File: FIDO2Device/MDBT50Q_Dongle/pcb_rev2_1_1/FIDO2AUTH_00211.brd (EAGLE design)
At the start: 19.7 x 35.6 mm, 36 parts, among them CN1 TE-1734028, CN2 IF_4PIN, CN3 IF_3PIN_SOL, CN5 IF_2PIN_SOL, SW1 SKRPACE010, SW2 SKTADAE010, U1 MDBT50Q-P1M, U2 XC6206P332MR-G, X1 NX3215SA-32.768K

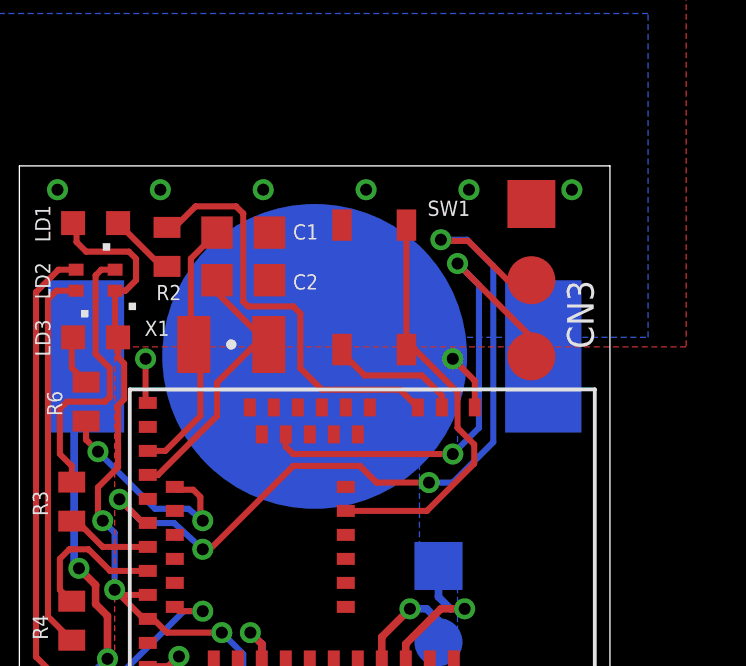
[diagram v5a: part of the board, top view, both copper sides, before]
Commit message: プリント基板設計データを修正
・TWIのブレイクアウトからGNDを削除（スペース削減のため）
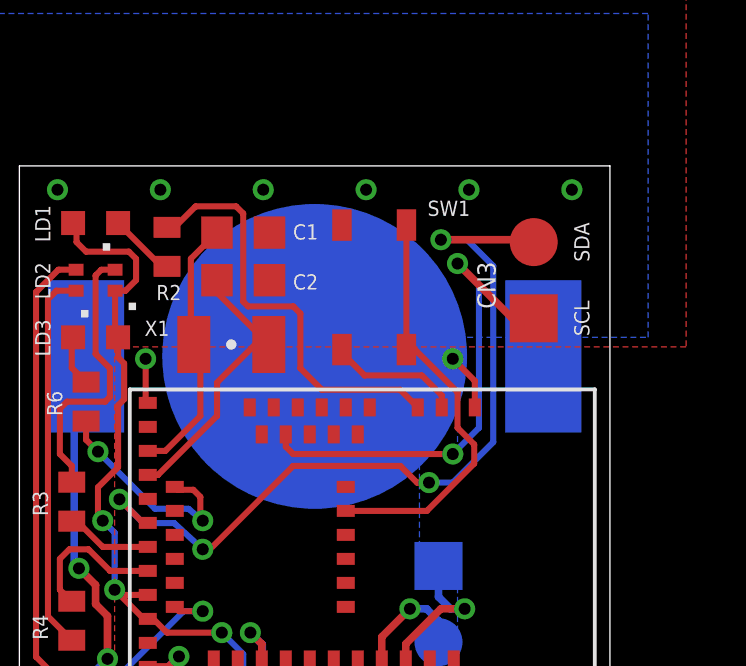
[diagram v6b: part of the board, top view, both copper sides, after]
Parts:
- CN3: value IF_3PIN_SOL -> IF_2PIN_SOL; device Connectors:SOLPAD_3PIN -> Connectors:SOLPAD_2PIN
- moved CN3 3.81 mm to (20.3, 30.5), turned to 90 degrees
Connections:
- net 0V: no longer CN3.1
- net TWI_SCL: now also CN3.1; no longer CN3.3
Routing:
- net TWI_SCL: track 17.2 -> 16.4 mm
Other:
- board text added: "SCL"
- board text added: "SDA"
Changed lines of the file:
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@@
 <setting verticaltext="up"/>
 </settings>
-<grid distance="0.05" unitdist="inch" unit="mil" style="lines" multiple="1" display="yes" altdistance="0.025" altunitdist="inch" altunit="inch"/>
+<grid distance="50" unitdist="mil" unit="mil" style="lines" multiple="1" display="yes" altdistance="0.025" altunitdist="inch" altunit="inch"/>
 <layers>
 <layer number="1" name="Top" color="4" fill="1" visible="yes" active="yes"/>
@@
 <text x="21.669375" y="14.605" size="0.508" layer="21" rot="R90" align="top-center">PCLK</text>
 <text x="21.669375" y="12.065" size="0.508" layer="21" rot="R90" align="top-center">PIO</text>
+<text x="21.669375" y="30.48" size="0.508" layer="21" rot="R90" align="top-center">SCL</text>
+<text x="21.669375" y="33.02" size="0.508" layer="21" rot="R90" align="top-center">SDA</text>
 </plain>
 <attributes>
@@
 </element>
 <element name="BAT1" library="Connectors" package="BAT-HLD-012-SMT" value="BAT-HLD-012-SMT" x="13.0175" y="29.21" rot="MR180"/>
-<element name="CN3" library="Connectors" package="SOLPAD_3PIN" value="IF_3PIN_SOL" x="20.240625" y="34.29" smashed="yes" rot="R270">
-<attribute name="NAME" x="21.43125" y="31.75" size="0.889" layer="25" ratio="11" rot="R270"/>
-<attribute name="VALUE" x="18.970625" y="35.56" size="0.889" layer="27" ratio="11" rot="R270" align="top-left"/>
-</element>
 <element name="LD3" library="Parts" package="CHIPLED_0603" value="APTD1608LSYCK" x="5.715" y="29.845" smashed="yes" rot="R180">
 <attribute name="NAME" x="4.206875" y="29.21" size="0.508" layer="25" rot="R90"/>
@@
 </element>
 <element name="CN5" library="Connectors" package="SOLPAD_2PIN" value="IF_2PIN_SOL" x="17.145" y="22.225" rot="MR270"/>
+<element name="CN3" library="Connectors" package="SOLPAD_2PIN" value="IF_2PIN_SOL" x="20.32" y="30.48" smashed="yes" rot="R90">
+<attribute name="NAME" x="19.05" y="30.7975" size="0.6096" layer="25" ratio="11" rot="R90"/>
+<attribute name="VALUE" x="21.59" y="29.21" size="0.889" layer="27" ratio="11" rot="R90" align="top-left"/>
+</element>
 </elements>
 <signals>
@@
 <contactref element="C11" pad="2"/>
 <contactref element="BAT1" pad="-"/>
-<contactref element="CN3" pad="1"/>
 <polygon width="0.4064" layer="16" isolate="0.4064" rank="3">
 <vertex x="1.905" y="-1.27"/>
@@
 <signal name="TWI_SCL">
 <contactref element="U1" pad="11"/>
-<contactref element="CN3" pad="3"/>
 <wire x1="12.055" y1="26.20375" x2="12.303125" y2="25.955625" width="0.2032" layer="1"/>
 <wire x1="12.055" y1="26.61" x2="12.055" y2="26.20375" width="0.2032" layer="1"/>
@@
 <via x="17.78" y="32.305625" extent="1-16" drill="0.4"/>
 <wire x1="18.494375" y1="31.59125" x2="17.78" y2="32.305625" width="0.2032" layer="16"/>
-<wire x1="20.240625" y1="29.21" x2="20.240625" y2="29.845" width="0.2032" layer="1"/>
-<wire x1="20.240625" y1="29.845" x2="17.78" y2="32.305625" width="0.2032" layer="1"/>
+<contactref element="CN3" pad="1"/>
+<wire x1="20.32" y1="30.48" x2="19.605625" y2="30.48" width="0.254" layer="1"/>
+<wire x1="19.605625" y1="30.48" x2="17.78" y2="32.305625" width="0.254" layer="1"/>
 </signal>
 <signal name="N$1">
@@
 <signal name="TWI_SDA">
 <contactref element="U1" pad="22"/>
-<contactref element="CN3" pad="2"/>
 <via x="6.50875" y="24.4475" extent="1-16" drill="0.4"/>
 <wire x1="7.44875" y1="23.65375" x2="7.455" y2="23.66" width="0.254" layer="1"/>
@@
 <wire x1="9.286875" y1="22.780625" x2="9.525" y2="22.780625" width="0.2032" layer="1"/>
 <via x="16.8275" y="25.003125" extent="1-16" drill="0.4"/>
-<wire x1="12.303125" y1="25.55875" x2="14.525625" y2="25.55875" width="0.2032" layer="1"/>
-<wire x1="14.525625" y1="25.55875" x2="15.08125" y2="25.003125" width="0.2032" layer="1"/>
-<wire x1="15.08125" y1="25.003125" x2="16.8275" y2="25.003125" width="0.2032" layer="1"/>
+<wire x1="12.303125" y1="25.55875" x2="15.875" y2="25.55875" width="0.2032" layer="1"/>
+<wire x1="15.875" y1="25.55875" x2="16.430625" y2="25.003125" width="0.2032" layer="1"/>
+<wire x1="16.430625" y1="25.003125" x2="16.8275" y2="25.003125" width="0.2032" layer="1"/>
 <wire x1="16.8275" y1="25.003125" x2="17.62125" y2="25.003125" width="0.2032" layer="16"/>
 <wire x1="17.62125" y1="25.003125" x2="18.970625" y2="26.3525" width="0.2032" layer="16"/>
@@
 <wire x1="18.970625" y1="32.22625" x2="18.0975" y2="33.099375" width="0.2032" layer="16"/>
 <wire x1="18.0975" y1="33.099375" x2="17.224375" y2="33.099375" width="0.2032" layer="16"/>
-<wire x1="20.240625" y1="31.75" x2="19.446875" y2="31.75" width="0.2032" layer="1"/>
-<wire x1="19.446875" y1="31.75" x2="18.1371875" y2="33.0596875" width="0.2032" layer="1"/>
-<wire x1="18.1371875" y1="33.0596875" x2="17.2640625" y2="33.0596875" width="0.2032" layer="1"/>
-<wire x1="17.2640625" y1="33.0596875" x2="17.224375" y2="33.099375" width="0.2032" layer="1"/>
 <wire x1="6.50875" y1="24.4475" x2="7.3025" y2="23.65375" width="0.2032" layer="16"/>
 <wire x1="7.3025" y1="23.65375" x2="8.334375" y2="23.65375" width="0.2032" layer="16"/>
 <wire x1="7.455" y1="23.66" x2="7.29625" y2="23.66" width="0.2032" layer="1"/>
 <wire x1="7.29625" y1="23.66" x2="6.50875" y2="24.4475" width="0.2032" layer="1"/>
+<contactref element="CN3" pad="2"/>
+<wire x1="20.32" y1="33.02" x2="20.240625" y2="33.099375" width="0.254" layer="1"/>
+<wire x1="20.240625" y1="33.099375" x2="17.224375" y2="33.099375" width="0.254" layer="1"/>
 </signal>
 <signal name="LED1">

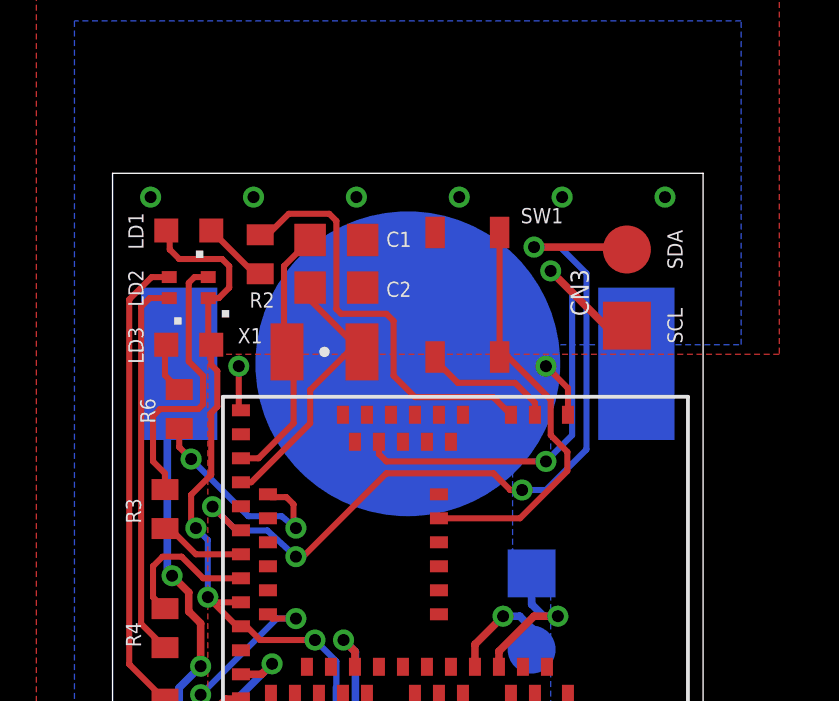
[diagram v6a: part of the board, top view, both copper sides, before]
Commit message: プリント基板設計データを修正
・TWI関連の配線を改善するための措置
・SW1を基板の端に移動
・LED1の配線を、P1.10 --> P0.27 へ変更
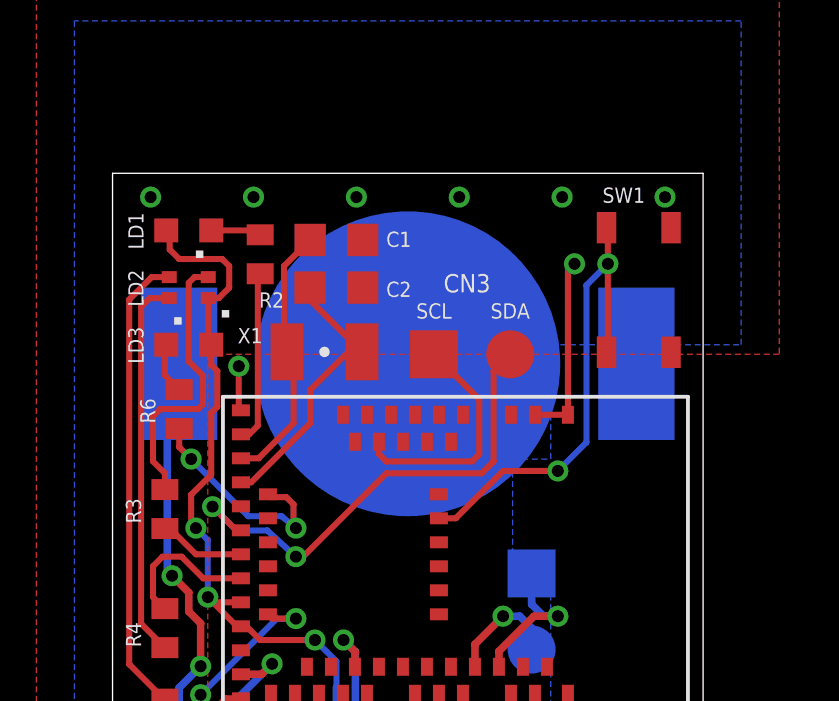
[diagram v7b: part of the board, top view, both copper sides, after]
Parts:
- moved CN3 6.50 mm to (13.9, 29.5), turned to 0 degrees
- moved SW1 5.72 mm to (20.7, 31.7), turned to 90 degrees
- turned R2 to 90 degrees
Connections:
- net LED1: now also U1.16; no longer U1.3
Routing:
- net TWI_SDA: track 27.5 -> 16.4 mm, vias 4 -> 2
- net LED1: track 14.2 -> 5.78 mm
- net TWI_SCL: track 16.4 -> 7.91 mm, vias 2 -> 0
- net SW1: track 14.0 -> 16.4 mm, vias 0 -> 2
- net N$11: track 2.23 -> 1.69 mm

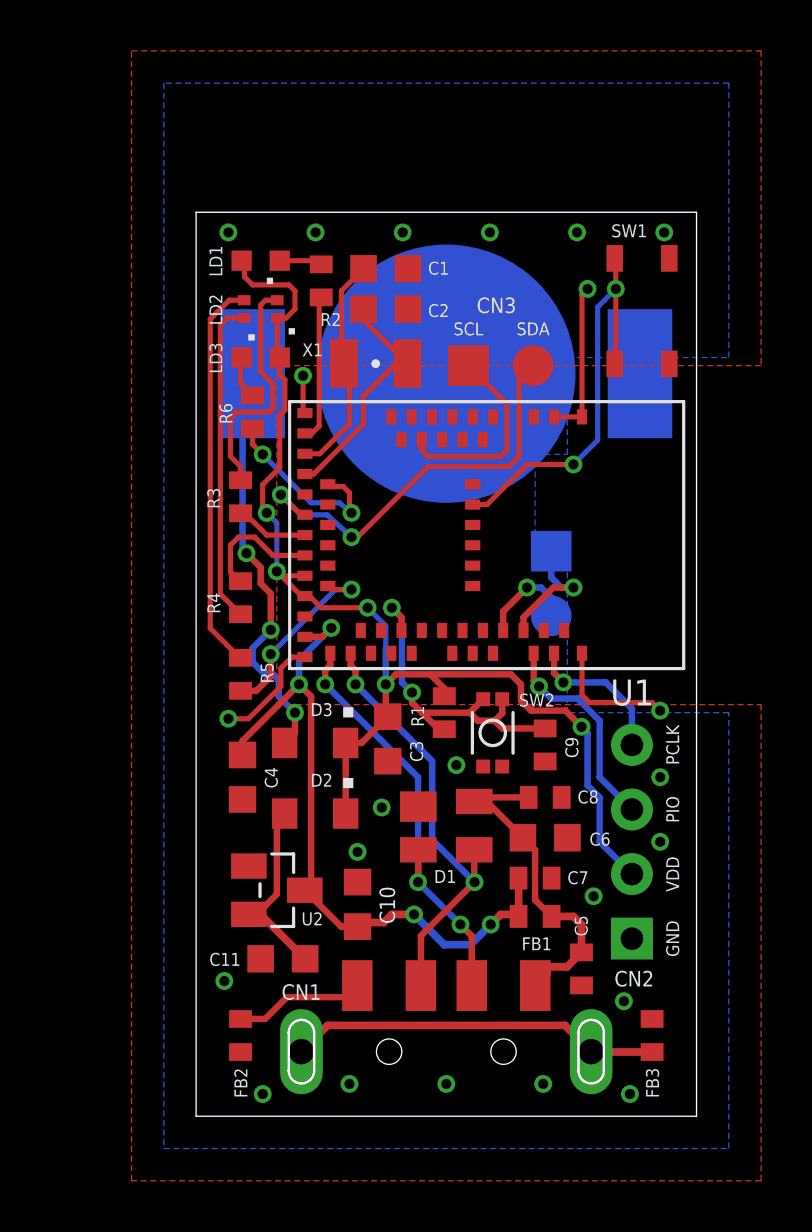
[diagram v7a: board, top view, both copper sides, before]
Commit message: プリント基板設計データを修正
・セキュアIC関連部品を搭載したパターンを作成
・TWI用のブレークアウトパターンを削除
・ATECC608Aの底面パッドパターンを削除
（ICの背面で配線する必要があるための措置）
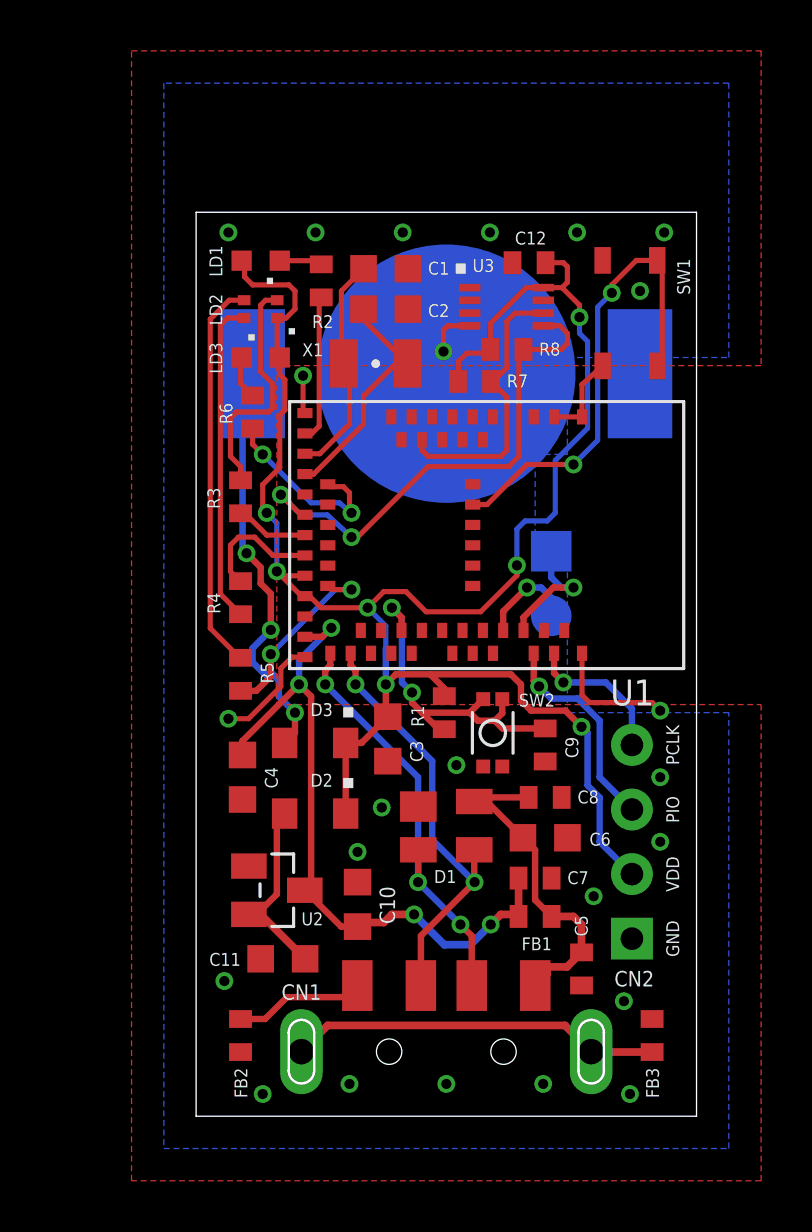
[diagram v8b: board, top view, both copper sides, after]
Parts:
- removed CN3: IF_2PIN_SOL, Connectors:SOLPAD_2PIN
- added C12: 0.1uF, Parts:C0402
- added R7, R8: 3.6k, Parts:R0402
- added U3: ATECC608A-MAHDA-S, ICs:DFN-2X3
- moved SW1 0.48 mm to (20.2, 31.6), turned to 270 degrees
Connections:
- net 0V: now also C12.2, U3.4
- net TWI_SCL: now also R7.1, U3.6; no longer CN3.1
- net TWI_SDA: now also R8.1, U3.5; no longer CN3.2
- net VDD_NRF: now also C12.1, R7.2, R8.2, U3.8
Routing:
- net VDD_NRF: track 46.9 -> 75.9 mm, vias 5 -> 7
- net TWI_SDA: track 16.4 -> 20.6 mm
- net TWI_SCL: track 7.91 -> 11.2 mm
- net SW1: track 16.4 -> 18.8 mm
- net 0V: track 17.2 -> 16.4 mm, vias 23 -> 24
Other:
- board text added: "P0.25"
- board text added: "P1.02"
- board text removed: "SCL"
- board text removed: "SDA"
